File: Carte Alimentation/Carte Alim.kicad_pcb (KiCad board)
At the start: 2 copper layers, 102.9 x 70.5 mm, 57 parts, among them K1 CONN_3, P1 CONN_2, P10 CONN_2, P11 CONN_2, P12 CONN_2, P13 CONN_4, P2 CONN_2, P3 CONN_2, P4 CONN_5, P5 CONN_1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

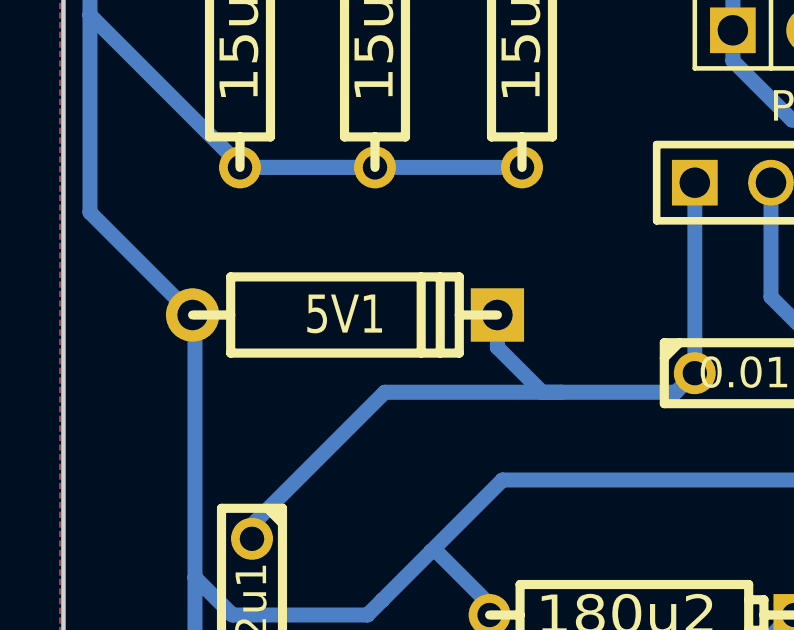
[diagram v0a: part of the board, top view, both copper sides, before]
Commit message: correction : remplacement d'une zener par une schottky
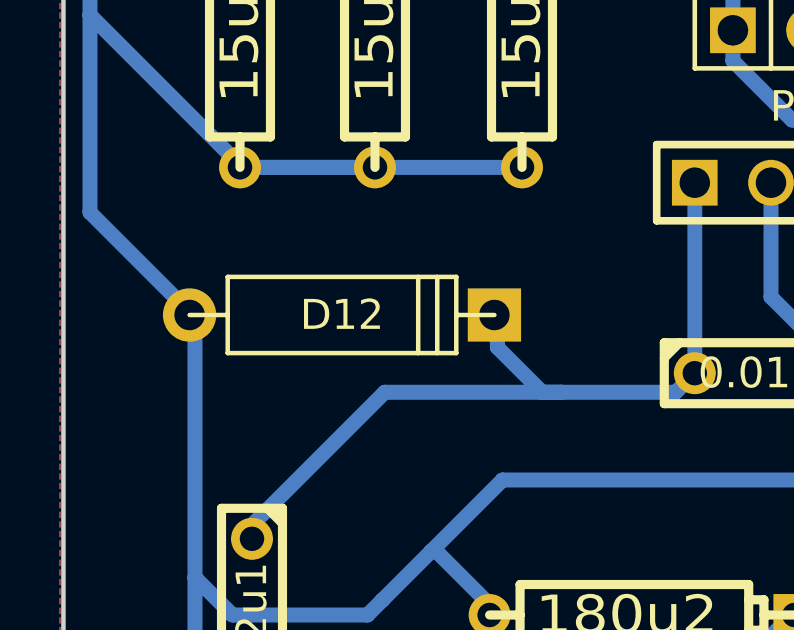
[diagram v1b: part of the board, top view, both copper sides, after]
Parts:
- removed 5V1: ZENER, D4
- added D12: DIODESCH, Discret:D4, F.Cu at (104.8, 130.0)

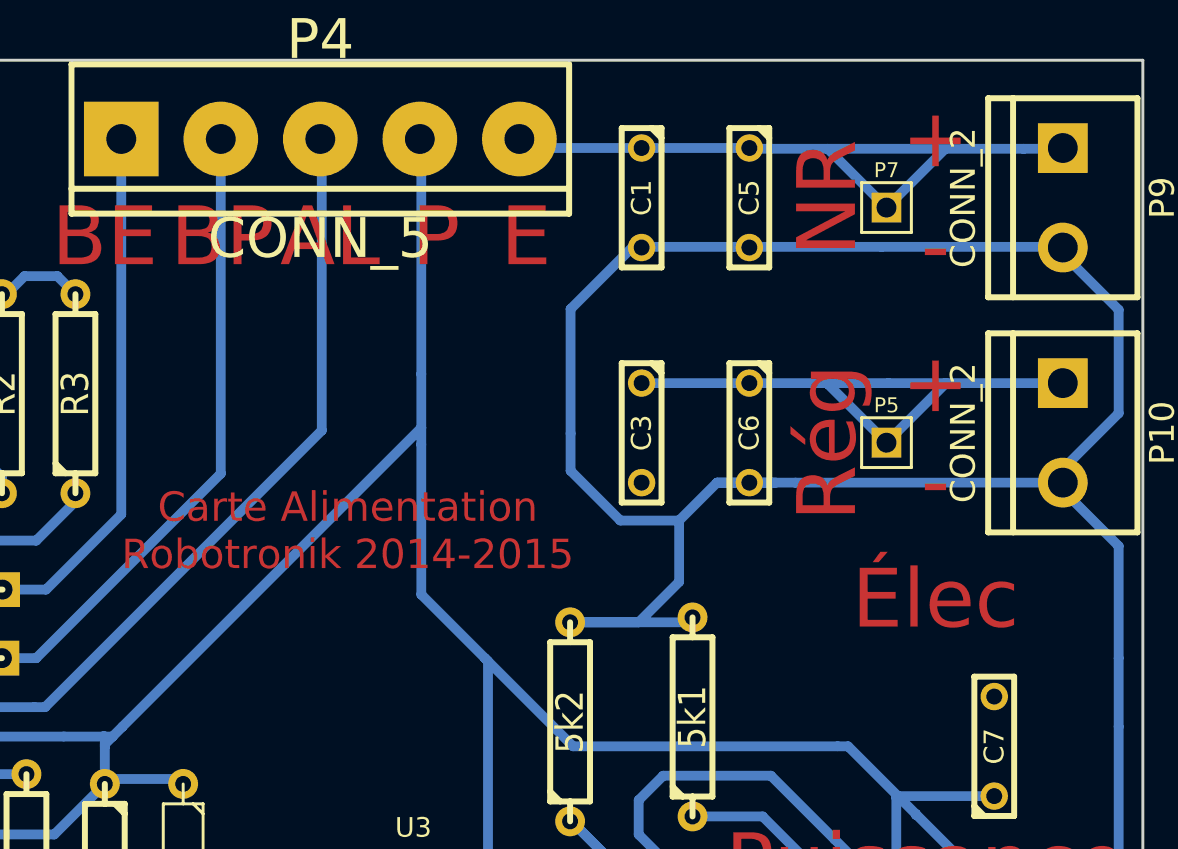
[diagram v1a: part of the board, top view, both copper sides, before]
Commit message: ajout régul 5V qui avait disparu
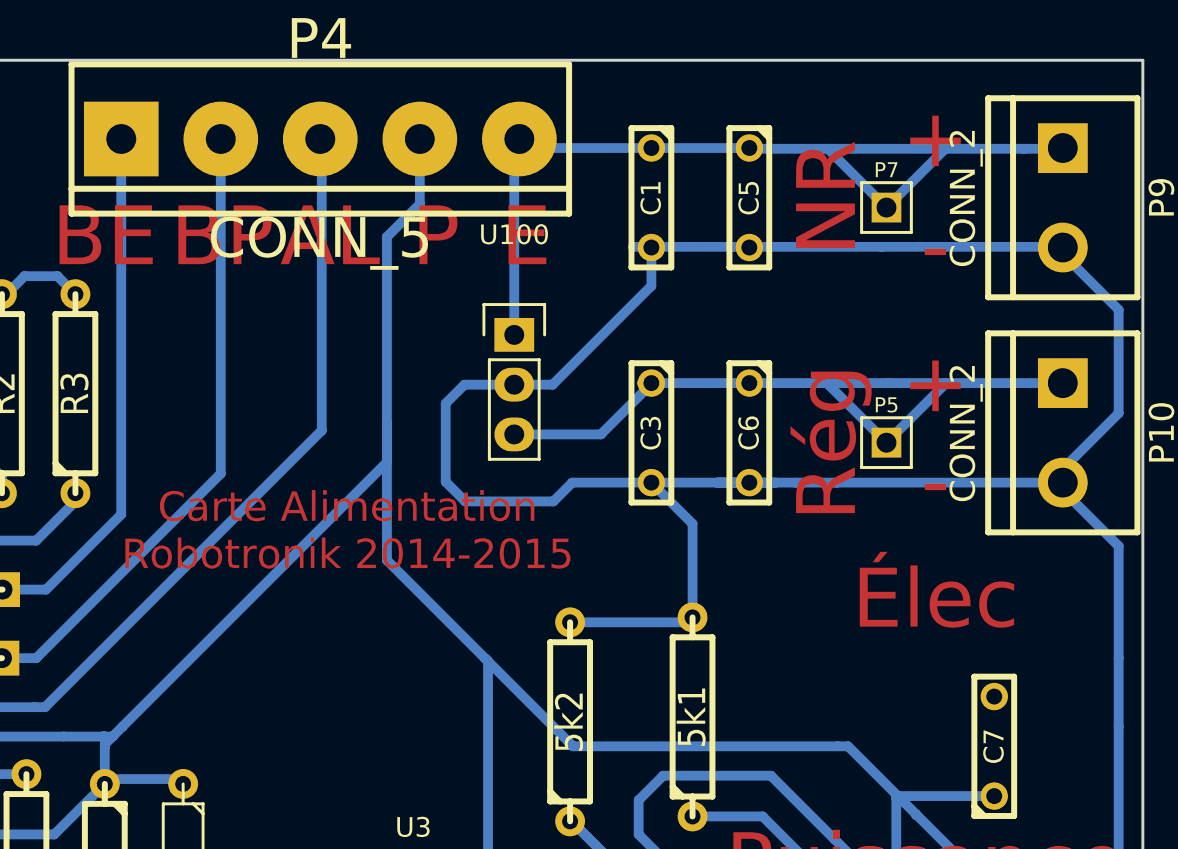
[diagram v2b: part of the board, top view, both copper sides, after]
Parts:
- added U100: 7905_CORRIGE, Pin_Headers:Pin_Header_Straight_1x03, F.Cu at (166.2, 90.5)
- moved C1 0.50 mm to (173.2, 83.5)
- moved C3 0.50 mm to (173.2, 95.5)
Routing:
- net GND: track 618.7 -> 631.1 mm
- net /alim_elec_non_regul: track 35.9 -> 46.0 mm
- net /alim_elec: track 30.0 -> 38.1 mm
